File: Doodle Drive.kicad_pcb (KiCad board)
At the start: 2 copper layers, 97.8 x 99.1 mm, 142 parts, among them J1 USB_B, J12 PINHD_1x4_Male, J15 PINHD_1x4_Male, J2 PINHD_1x4_Male, J6 PINHD_1x2_Male, J8 PINHD_1x4_Male, J9 PINHD_1x4_Male, SW1 Push_Button, SW2 Push_Button, SW3 Push_Button, U1 STM32F411RETx, U2 DRV8825PWP, U3 DRV8825PWP, U4 DRV8825PWP, U5 DRV8825PWP, U6 AP7343-30W5-7, U7 CP2102N-Axx-xQFN28, Y1 32.768KHz ±20ppm 12.5pF, Y2 25MHZ 9PF

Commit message: fixed voltage dividers, roughly arrangenged components on pcb, set up 3V3 and GND area
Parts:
- removed R20, R36: 1k, Resistor_SMD:R_0805_2012Metric
- removed RV4: R_Potentiometer, Potentiometer_THT:Potentiometer_ACP_CA6-H2,5_Horizontal
- removed TP6, TP8: TestPoint, TestPoint:TestPoint_Pad_D2.5mm
- added R10: 1k, Resistor_SMD:R_0805_2012Metric, F.Cu at (168.4, 89.5)
- added R11: 1k, Resistor_SMD:R_0805_2012Metric, F.Cu at (147.6, 110.5)
- added RV2: R_Potentiometer, Potentiometer_THT:Potentiometer_ACP_CA6-H2,5_Horizontal, F.Cu at (171.4, 89.0)
- added TP2: TestPoint, TestPoint:TestPoint_Pad_D2.5mm, F.Cu at (147.3, 133.3)
- added TP5: TestPoint, TestPoint:TestPoint_Pad_D2.5mm, F.Cu at (146.0, 106.7)
- moved R8 227.6 mm to (145.7, 73.7)
- moved R3 226.5 mm to (145.7, 76.2)
- moved TP23 224.7 mm to (188.0, 105.4)
- moved TP24 224.7 mm to (188.0, 110.0)
- moved TP25 224.7 mm to (188.0, 114.5)
- moved TP26 224.7 mm to (188.0, 119.1)
- moved TP10 223.2 mm to (188.0, 48.8)
- moved TP11 222.0 mm to (188.0, 62.2)
- moved TP9 221.4 mm to (188.0, 58.4)
- moved TP27 221.1 mm to (188.0, 123.2)
- moved TP28 221.1 mm to (188.0, 127.7)
- moved TP29 221.1 mm to (188.0, 132.3)
- moved D4 220.3 mm to (182.5, 69.8)
- moved R4 220.2 mm to (137.9, 65.3)
- moved R2 219.6 mm to (138.4, 69.8)
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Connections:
- J6 pad 1: Net-(J6-Pad1) -> +5V
- J6 pad 2: +5V -> PB6
- R5 pad 1: Net-(R5-Pad1) -> Net-(U2-AVREF)
- R7 pad 1: Net-(R7-Pad1) -> Net-(U3-AVREF)
- RV1 pad 1: unconnected-(RV1-Pad1) -> Net-(U2-AVREF)
- RV1 pad 2: Net-(R5-Pad1) -> GND
- RV1 pad 3: Net-(U2-AVREF) -> unconnected-(RV1-Pad3)
- RV3 pad 1: unconnected-(RV3-Pad1) -> Net-(U5-AVREF)
- RV3 pad 2: Net-(R20-Pad1) -> GND
- RV3 pad 3: Net-(U4-AVREF) -> unconnected-(RV3-Pad3)
- RV5 pad 1: Net-(J6-Pad1) -> unconnected-(RV5-Pad1)
- RV5 pad 2: PB6 -> GND
- RV5 pad 3: unconnected-(RV5-Pad3) -> PB6
- RV6 pad 1: unconnected-(RV6-Pad1) -> Net-(U3-AVREF)
- RV6 pad 2: Net-(R7-Pad1) -> GND
- RV6 pad 3: Net-(U3-AVREF) -> unconnected-(RV6-Pad3)
- TP1 pad 1: Net-(R5-Pad1) -> Net-(U2-AVREF)
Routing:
- net +3V3: track 0.00 -> 24.4 mm
- net +5V: track 0.00 -> 6.86 mm
- net Net-(U7-~{RST}): track 0.00 -> 2.54 mm
- net Net-(U7-VDD): track 0.00 -> 2.54 mm
- added copper zone on B.Cu, net +3V3

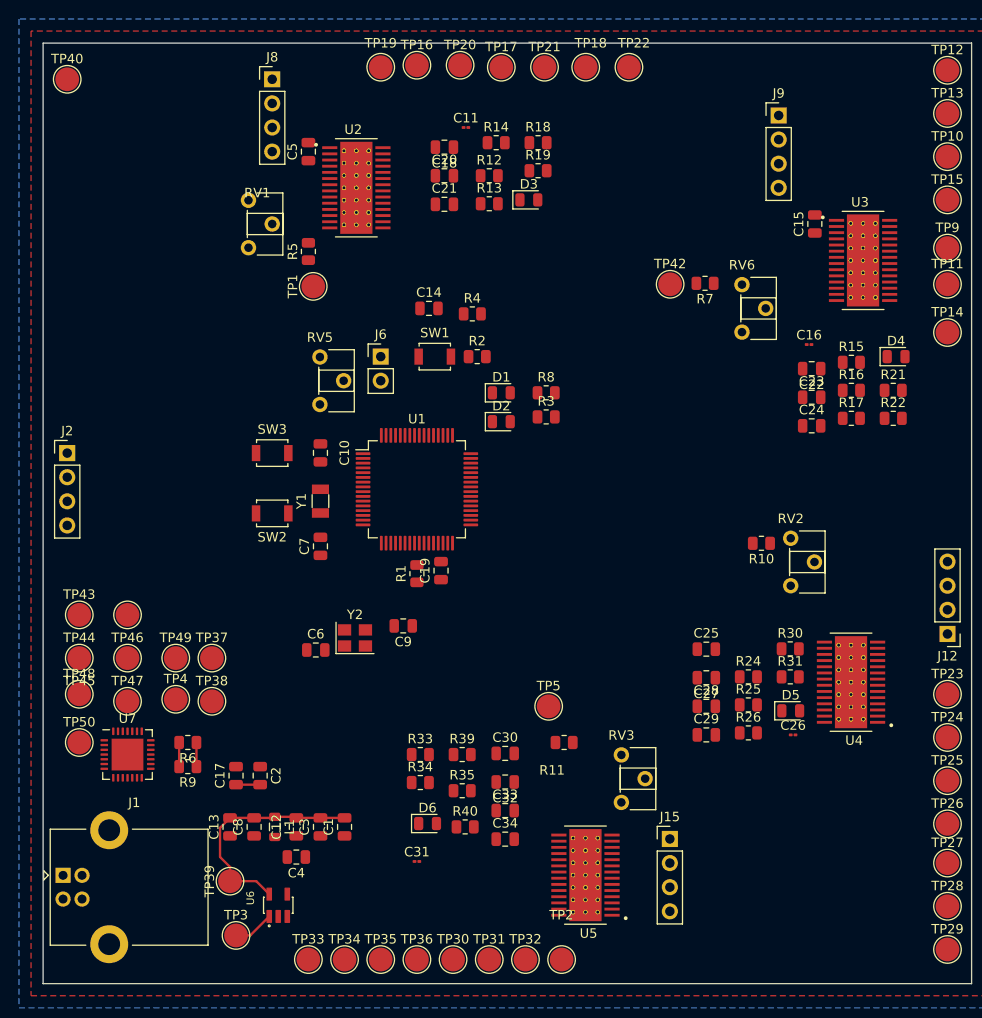
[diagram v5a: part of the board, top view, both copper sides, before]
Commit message: routed some paths on schematic. need to rearrange driver pins and come up with solution with motor poer supply
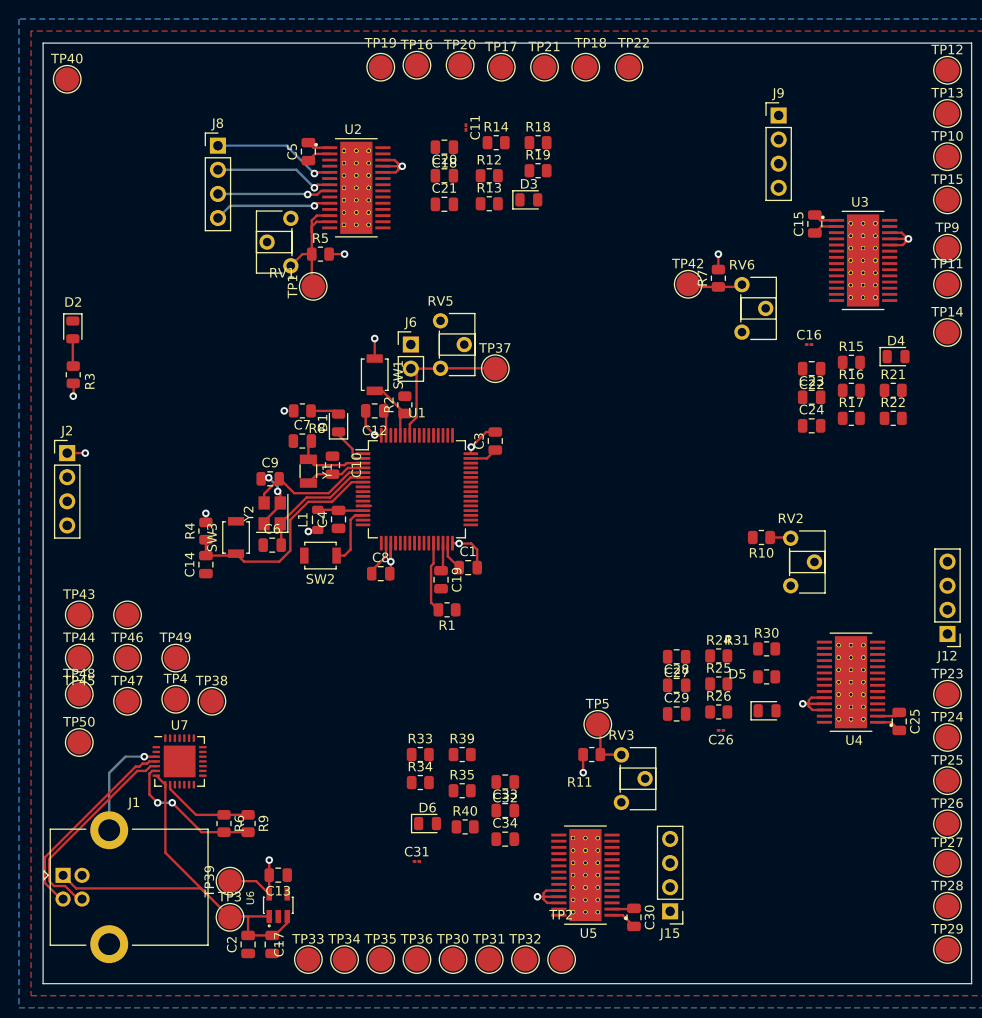
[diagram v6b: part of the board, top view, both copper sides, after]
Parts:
- moved R3 50.0 mm to (95.9, 71.8), turned to -90 degrees
- moved D2 46.2 mm to (95.8, 67.0), turned to -90 degrees
- moved C3 44.6 mm to (140.3, 78.7)
- moved C12 44.6 mm to (127.6, 75.6), turned to 180 degrees
- moved TP37 42.7 mm to (140.3, 71.1)
- moved R4 36.2 mm to (109.9, 88.2), turned to 90 degrees
- moved C4 35.8 mm to (123.8, 87.0), turned to 90 degrees
- moved C14 35.8 mm to (109.9, 91.8), turned to 90 degrees
- moved L1 32.7 mm to (121.6, 87.0), turned to 90 degrees
- moved C1 30.3 mm to (137.5, 92.1), turned to 0 degrees
- moved C8 29.8 mm to (128.3, 92.7), turned to 0 degrees
- moved R8 25.7 mm to (120.0, 75.6), turned to 180 degrees
- moved C30 22.0 mm to (154.9, 128.9), turned to -90 degrees
- moved C25 21.7 mm to (182.9, 108.3), turned to -90 degrees
- moved C9 20.9 mm to (116.6, 82.7), turned to 0 degrees
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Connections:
- C10 pad 1: PC13 -> PC15
- J12 pad 3: Net-(U4-BOUT1) -> Net-(U4-BOUT2)
- J12 pad 4: Net-(U4-BOUT2) -> Net-(U4-BOUT1)
- J15 pad 3: Net-(U5-BOUT1) -> Net-(U5-BOUT2)
- J15 pad 4: Net-(U5-BOUT2) -> Net-(U5-BOUT1)
- J8 pad 3: Net-(U2-BOUT1) -> Net-(U2-BOUT2)
- J8 pad 4: Net-(U2-BOUT2) -> Net-(U2-BOUT1)
- J9 pad 3: Net-(U3-BOUT1) -> Net-(U3-BOUT2)
- J9 pad 4: Net-(U3-BOUT2) -> Net-(U3-BOUT1)
- R4 pad 2: +3.3V -> +3V3
- SW1 pad 1: +3.3V -> +3V3
- U2 pad 24: +5V -> +3V3
- U2 pad 25: +5V -> +3V3
- U2 pad 26: +5V -> +3V3
- U3 pad 24: +5V -> +3V3
- U3 pad 25: +5V -> +3V3
- U3 pad 26: +5V -> +3V3
- U4 pad 24: +5V -> +3V3
- U4 pad 25: +5V -> +3V3
- U4 pad 26: +5V -> +3V3
- U5 pad 24: +5V -> +3V3
- U5 pad 25: +5V -> +3V3
- U5 pad 26: +5V -> +3V3
- Y1 pad 1: PC13 -> PC15
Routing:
- net +3V3: track 24.4 -> 65.8 mm, vias 0 -> 18
- net +5V: track 6.86 -> 45.5 mm
- net GND: track 0.00 -> 32.6 mm, vias 0 -> 3
- net NRST: track 0.00 -> 24.0 mm
- net Net-(J1-D+): track 0.00 -> 21.9 mm
- net Net-(J1-D-): track 0.00 -> 21.2 mm
- net PB6: track 0.00 -> 16.5 mm
- net Net-(U2-AVREF): track 0.00 -> 14.5 mm
- net PH0: track 0.00 -> 13.6 mm
- net Net-(U2-AOUT1): track 0.00 -> 13.0 mm, vias 0 -> 1
- net PH1: track 0.00 -> 13.0 mm
- net Net-(U2-AOUT2): track 0.00 -> 12.7 mm, vias 0 -> 1
- net Net-(U7-VDD): track 2.54 -> 15.1 mm, vias 0 -> 2
- net Net-(U2-BOUT1): track 0.00 -> 12.4 mm, vias 0 -> 1
- net Net-(U2-BOUT2): track 0.00 -> 12.0 mm, vias 0 -> 1
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
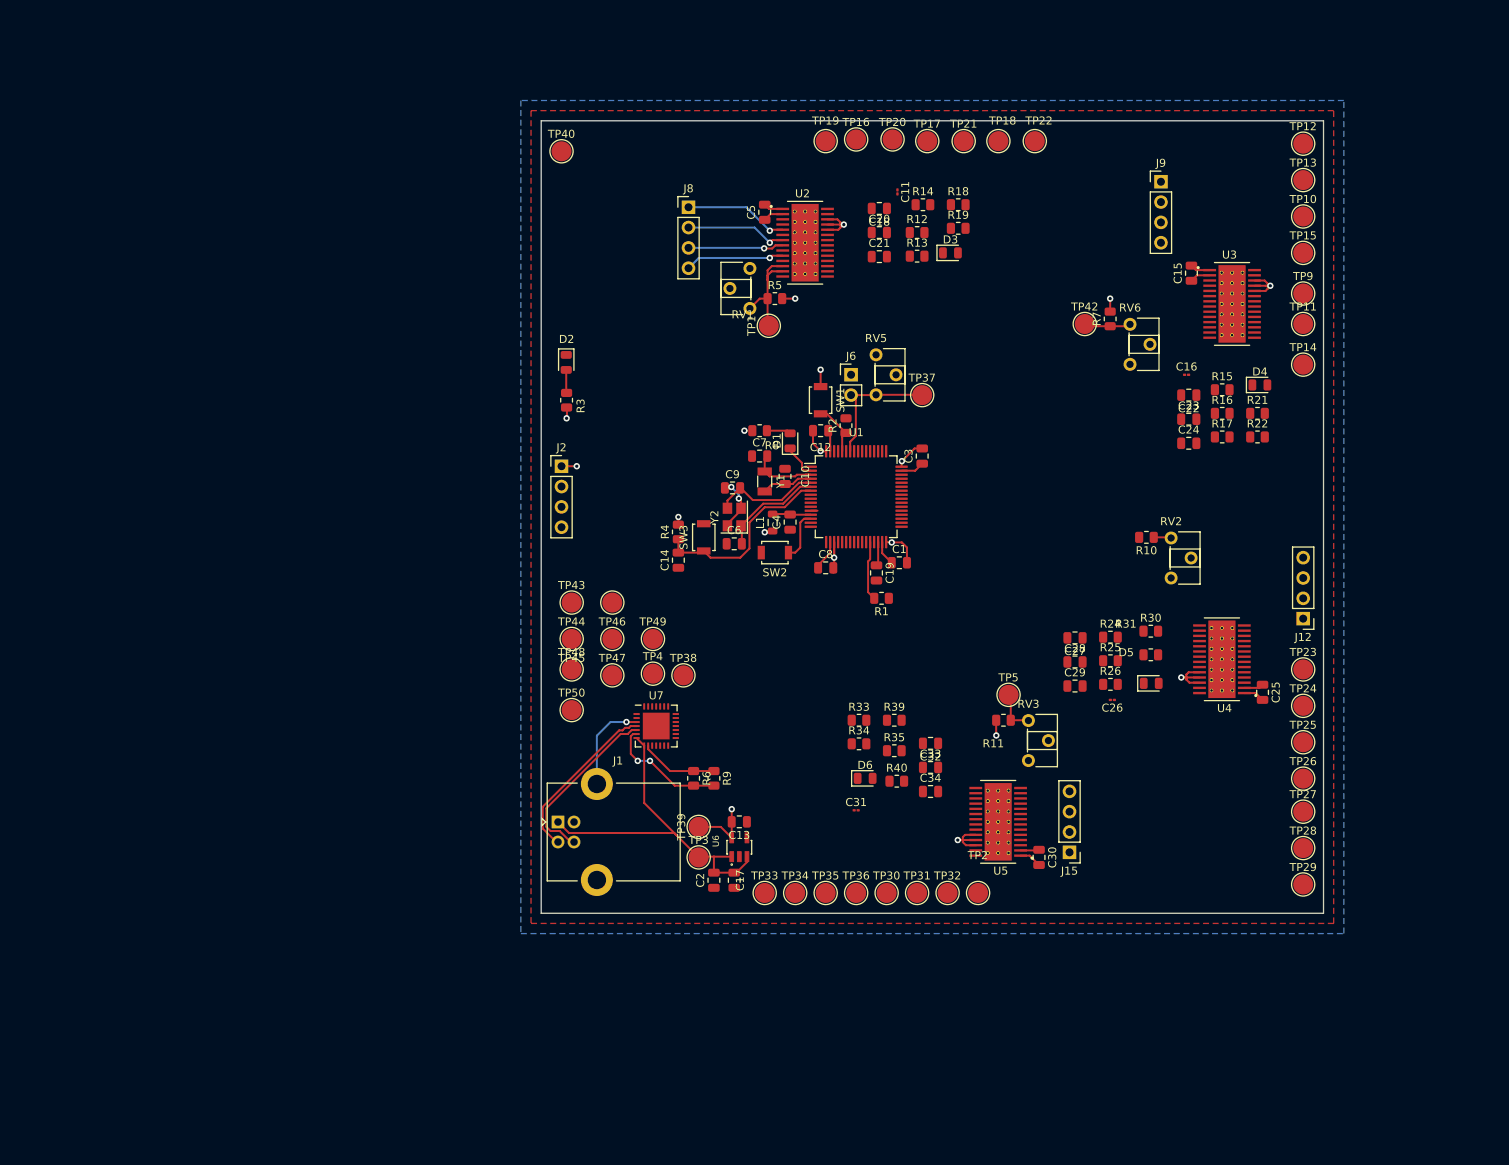
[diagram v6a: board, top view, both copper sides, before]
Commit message: temporarly detached testpoints
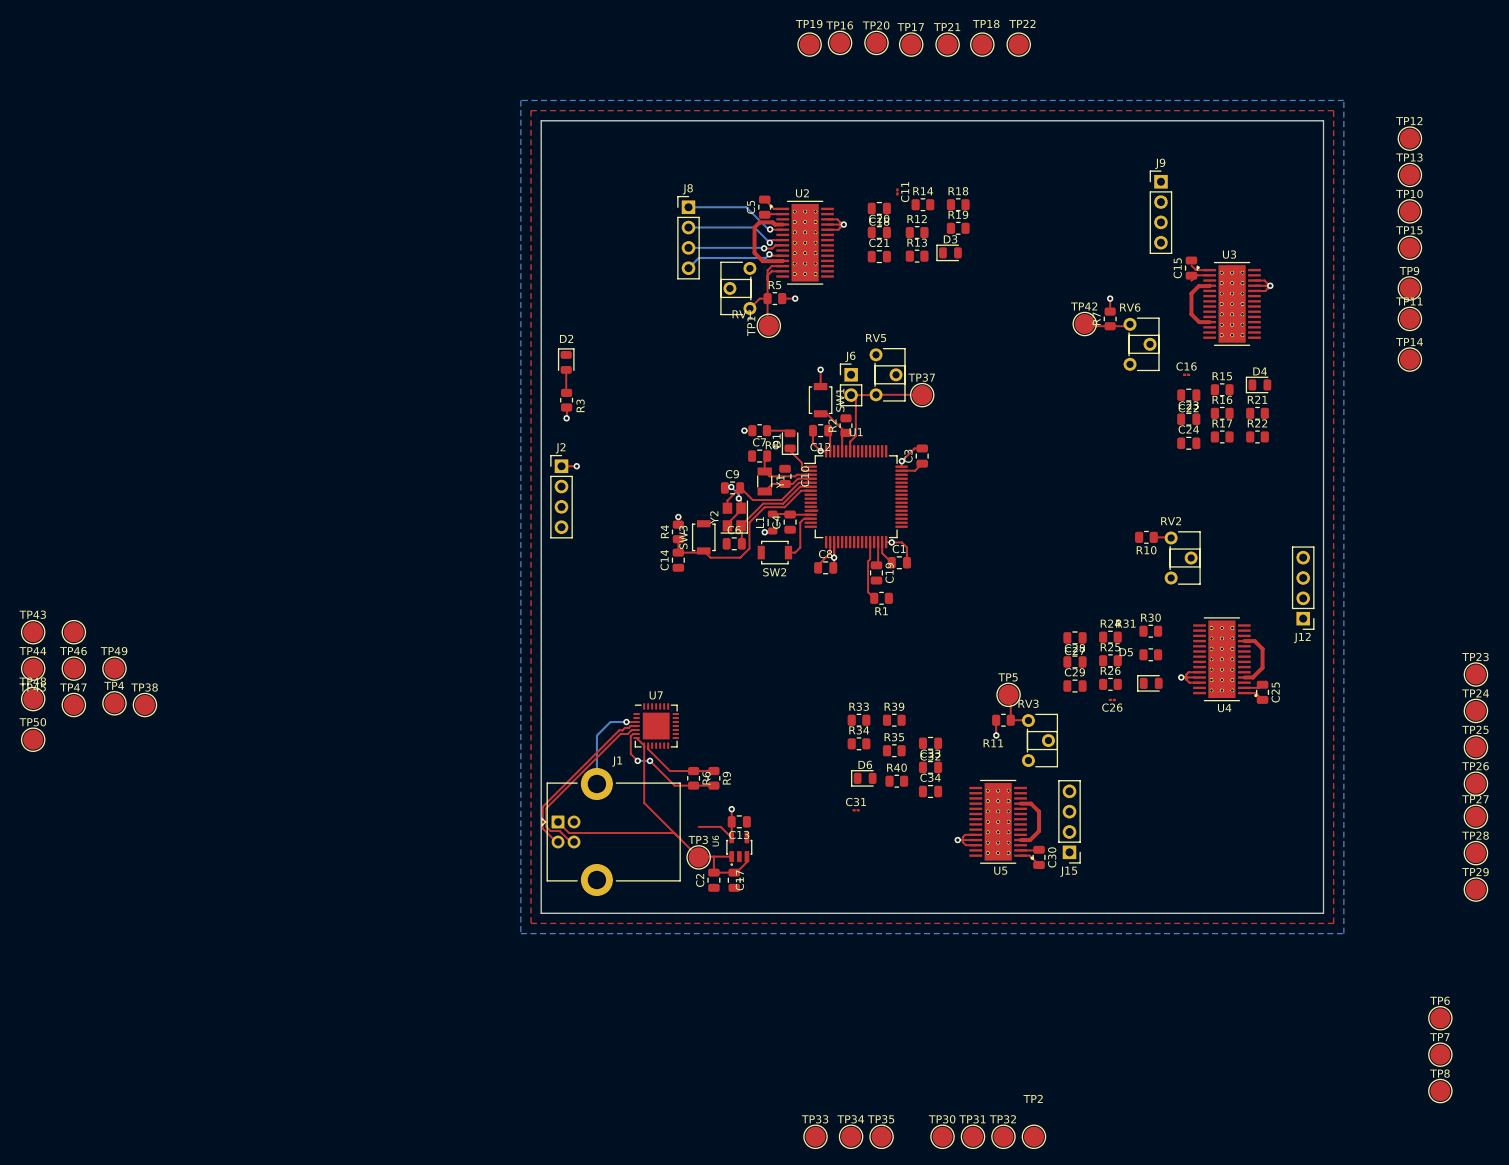
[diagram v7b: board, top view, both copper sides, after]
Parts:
- removed TP36, TP39, TP40: TestPoint, TestPoint:TestPoint_Pad_D2.5mm
- added TP6: TestPoint, TestPoint:TestPoint_Pad_D2.5mm, F.Cu at (205.1, 149.0)
- added TP7: TestPoint, TestPoint:TestPoint_Pad_D2.5mm, F.Cu at (205.1, 153.6)
- added TP8: TestPoint, TestPoint:TestPoint_Pad_D2.5mm, F.Cu at (205.1, 158.1)
- moved TP38 67.4 mm to (43.2, 109.9)
- moved TP4 67.4 mm to (39.4, 109.6)
- moved TP43 67.4 mm to (29.2, 100.8)
- moved TP44 67.4 mm to (29.2, 105.3)
- moved TP45 67.4 mm to (34.3, 100.8)
- moved TP46 67.4 mm to (34.3, 105.3)
- moved TP47 67.4 mm to (34.3, 109.9)
- moved TP48 67.4 mm to (29.2, 109.1)
- moved TP49 67.4 mm to (39.4, 105.3)
- moved TP50 67.4 mm to (29.2, 114.2)
- moved TP2 31.3 mm to (154.3, 163.8)
- moved TP30 31.3 mm to (142.9, 163.8)
- moved TP31 31.3 mm to (146.7, 163.8)
- moved TP32 31.3 mm to (150.5, 163.8)
- moved TP34 31.3 mm to (131.4, 163.8)
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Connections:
- C11 pad 1: VM -> +15V
- C16 pad 1: VM -> +15V
- C18 pad 2: VM -> +15V
- C20 pad 1: VM -> +15V
- C21 pad 1: VM -> +15V
- C22 pad 2: VM -> +15V
- C23 pad 1: VM -> +15V
- C24 pad 1: VM -> +15V
- C26 pad 1: VM -> +15V
- C27 pad 2: VM -> +15V
- C28 pad 1: VM -> +15V
- C29 pad 1: VM -> +15V
- C31 pad 1: VM -> +15V
- C32 pad 2: VM -> +15V
- C33 pad 1: VM -> +15V
- C34 pad 1: VM -> +15V
- R14 pad 2: VM -> +15V
- R17 pad 2: VM -> +15V
- R26 pad 2: VM -> +15V
- R35 pad 2: VM -> +15V
- R4 pad 2: +3V3 -> +3.3V
- SW1 pad 1: +3V3 -> +3.3V
- TP10 pad 1: NSLEEP1 -> unconnected-(TP10-Pad1)
- TP11 pad 1: NFAULT1 -> unconnected-(TP11-Pad1)
- TP12 pad 1: NHOME1 -> unconnected-(TP12-Pad1)
- TP13 pad 1: NENBL1 -> unconnected-(TP13-Pad1)
- TP14 pad 1: PA2 -> unconnected-(TP14-Pad1)
- TP15 pad 1: DIR1 -> unconnected-(TP15-Pad1)
- TP16 pad 1: DIR2 -> unconnected-(TP16-Pad1)
- TP17 pad 1: PA9 -> unconnected-(TP17-Pad1)
- TP18 pad 1: NENBL2 -> unconnected-(TP18-Pad1)
- TP19 pad 1: NHOME2 -> unconnected-(TP19-Pad1)
- TP20 pad 1: NFAULT2 -> unconnected-(TP20-Pad1)
- TP21 pad 1: NSLEEP2 -> unconnected-(TP21-Pad1)
- TP22 pad 1: NRESET2 -> unconnected-(TP22-Pad1)
- TP23 pad 1: DIR3 -> unconnected-(TP23-Pad1)
- TP24 pad 1: PB5 -> unconnected-(TP24-Pad1)
- TP25 pad 1: NENBL3 -> unconnected-(TP25-Pad1)
- TP26 pad 1: NHOME3 -> unconnected-(TP26-Pad1)
- TP27 pad 1: NFAULT3 -> unconnected-(TP27-Pad1)
- TP28 pad 1: NSLEEP3 -> unconnected-(TP28-Pad1)
- TP29 pad 1: NRESET3 -> unconnected-(TP29-Pad1)
- TP30 pad 1: DIR4 -> unconnected-(TP30-Pad1)
- TP31 pad 1: PB14 -> unconnected-(TP31-Pad1)
- TP32 pad 1: NENBL4 -> unconnected-(TP32-Pad1)
- TP33 pad 1: NHOME4 -> unconnected-(TP33-Pad1)
- TP34 pad 1: NFAULT4 -> +15V
- TP35 pad 1: NSLEEP4 -> +3V3
- TP9 pad 1: NRESET1 -> unconnected-(TP9-Pad1)
- U2 pad 11: VM -> +15V
- U2 pad 4: VM -> +15V
- U3 pad 11: VM -> +15V
- U3 pad 4: VM -> +15V
- U4 pad 11: VM -> +15V
- U4 pad 4: VM -> +15V
- U5 pad 11: VM -> +15V
- U5 pad 4: VM -> +15V
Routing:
- net +15V: track 0.00 -> 34.7 mm
- net +3.3V: track 0.00 -> 3.06 mm, vias 0 -> 2
- net +3V3: track 65.8 -> 62.8 mm, vias 18 -> 16

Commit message: routet Motor Driver modules, reattached and placed testpoints
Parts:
- removed TP47, TP48, TP49, TP50: TestPoint, TestPoint:TestPoint_Pad_D2.5mm
- added TP36: TestPoint, TestPoint:TestPoint_Pad_D2.5mm, F.Cu at (11.4, -35.6)
- added TP39: TestPoint, TestPoint:TestPoint_Pad_D2.5mm, F.Cu at (19.1, -34.9)
- added TP40: TestPoint, TestPoint:TestPoint_Pad_D2.5mm, F.Cu at (7.62, -38.1)
- added TP41: TestPoint, TestPoint:TestPoint_Pad_D2.5mm, F.Cu at (7.62, -33.7)
- C11, C16, C26, C31: footprint Capacitor_SMD:C_01005_0402Metric -> Capacitor_SMD:C_0402_1005Metric
- moved TP8 287.3 mm to (40.7, -77.5), turned to 90 degrees
- moved TP7 286.3 mm to (41.3, -81.3), turned to 90 degrees
- moved TP6 281.6 mm to (36.9, -76.8), turned to 90 degrees
- moved TP35 260.0 mm to (2.54, -59.7)
- moved TP2 248.5 mm to (54.0, -63.5)
- moved TP26 240.9 mm to (49.5, -60.3)
- moved TP24 238.6 mm to (45.7, -62.9)
- moved TP29 237.7 mm to (39.4, -33.0)
- moved TP28 236.9 mm to (35.6, -32.4)
- moved TP25 235.9 mm to (44.5, -53.3)
- moved TP14 235.2 mm to (19.0, -81.9)
- moved TP27 228.6 mm to (43.2, -33.0)
- moved TP15 227.2 mm to (16.5, -79.4)
- moved TP32 226.6 mm to (31.8, -29.2)
- moved TP13 224.8 mm to (12.7, -78.7)
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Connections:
- R4 pad 2: +3.3V -> +3V3
- SW1 pad 1: +3.3V -> +3V3
- TP10 pad 1: unconnected-(TP10-Pad1) -> NFAULT1
- TP11 pad 1: unconnected-(TP11-Pad1) -> NSLEEP1
- TP12 pad 1: unconnected-(TP12-Pad1) -> NRESET1
- TP13 pad 1: unconnected-(TP13-Pad1) -> DIR2
- TP14 pad 1: unconnected-(TP14-Pad1) -> PA9
- TP15 pad 1: unconnected-(TP15-Pad1) -> NENBL2
- TP16 pad 1: unconnected-(TP16-Pad1) -> NHOME2
- TP17 pad 1: unconnected-(TP17-Pad1) -> NFAULT2
- TP18 pad 1: unconnected-(TP18-Pad1) -> NSLEEP2
- TP19 pad 1: unconnected-(TP19-Pad1) -> NRESET2
- TP20 pad 1: unconnected-(TP20-Pad1) -> DIR3
- TP21 pad 1: unconnected-(TP21-Pad1) -> PB5
- TP22 pad 1: unconnected-(TP22-Pad1) -> NENBL3
- TP23 pad 1: unconnected-(TP23-Pad1) -> NHOME3
- TP24 pad 1: unconnected-(TP24-Pad1) -> NFAULT3
- TP25 pad 1: unconnected-(TP25-Pad1) -> NSLEEP3
- TP26 pad 1: unconnected-(TP26-Pad1) -> NRESET3
- TP27 pad 1: unconnected-(TP27-Pad1) -> DIR4
- TP28 pad 1: unconnected-(TP28-Pad1) -> PB14
- TP29 pad 1: unconnected-(TP29-Pad1) -> NENBL4
- TP30 pad 1: unconnected-(TP30-Pad1) -> NHOME4
- TP31 pad 1: unconnected-(TP31-Pad1) -> NFAULT4
- TP32 pad 1: unconnected-(TP32-Pad1) -> NSLEEP4
- TP33 pad 1: unconnected-(TP33-Pad1) -> NRESET4
- TP38 pad 1: PC6 -> NRTS
- TP43 pad 1: NRTS -> NDCD
- TP44 pad 1: NCTS -> NRI
- TP45 pad 1: NDSR -> PC12
- TP46 pad 1: NDTR -> NSUSPEND
- TP6 pad 1: unconnected-(TP6-Pad1) -> DIR1
- TP7 pad 1: unconnected-(TP7-Pad1) -> PA2
- TP8 pad 1: unconnected-(TP8-Pad1) -> NENBL1
- TP9 pad 1: unconnected-(TP9-Pad1) -> NHOME1
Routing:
- net +15V: track 34.7 -> 104.0 mm, vias 0 -> 8
- net GND: track 32.6 -> 68.7 mm
- net NHOME1: track 0.00 -> 15.5 mm, vias 0 -> 2
- net Net-(U4-ISENA): track 0.00 -> 13.3 mm, vias 0 -> 2
- net Net-(U3-ISENA): track 0.00 -> 13.3 mm, vias 0 -> 2
- net Net-(U5-ISENA): track 0.00 -> 13.1 mm
- net NSLEEP3: track 0.00 -> 12.4 mm
- net NSLEEP4: track 0.00 -> 12.3 mm, vias 0 -> 2
- net Net-(U2-ISENB): track 0.00 -> 11.7 mm, vias 0 -> 2
- net NSLEEP2: track 0.00 -> 10.7 mm
- net Net-(U3-ISENB): track 0.00 -> 10.6 mm, vias 0 -> 2
- net PC7: track 0.00 -> 10.4 mm
- net Net-(U4-AVREF): track 2.21 -> 12.6 mm
- net NRESET2: track 0.00 -> 10.4 mm
- net NENBL3: track 0.00 -> 10.0 mm, vias 0 -> 2
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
